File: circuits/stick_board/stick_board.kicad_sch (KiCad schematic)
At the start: 22 parts, among them J1 Conn_01x13_Pin, M2 Motor_DC, Q2 AO3400A, U1 GULI, U2 GULI, U5 DRV5055A1xDBZxQ1, U6 DRV5055A1xDBZxQ1

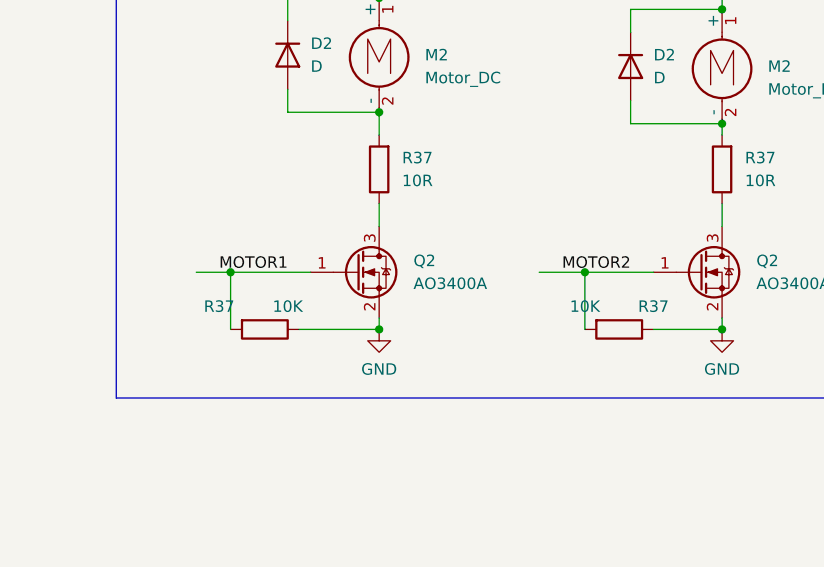
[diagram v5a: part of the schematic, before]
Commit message: 马达驱动增加栅极电阻
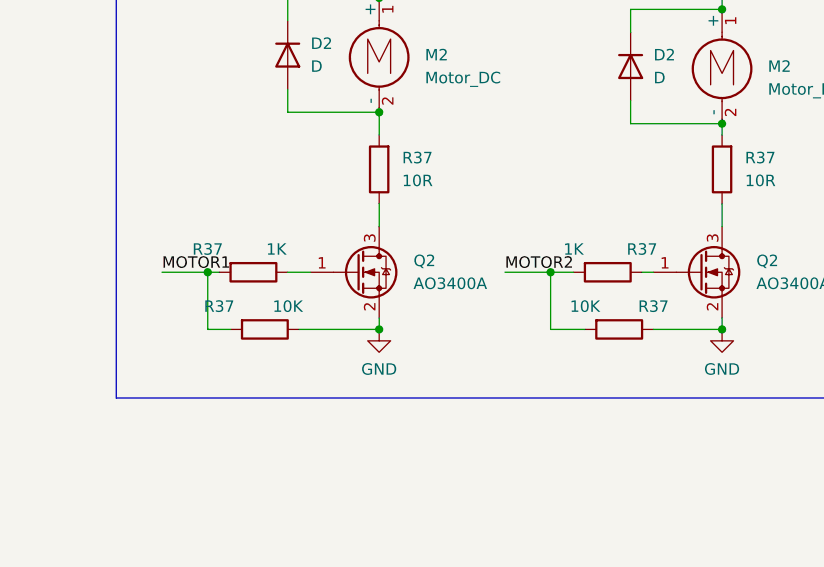
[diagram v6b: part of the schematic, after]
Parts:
- added R37 (x2): 1K, Resistor_SMD:R_0805_2012Metric_Pad1.20x1.40mm_HandSolder, symbol Device:R
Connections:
- net MOTOR1: now also R37.2; no longer Q2.1 (G)
- net MOTOR2: now also R37.2; no longer Q2.1 (G)
- new net: Q2.1 (G), R37.1 (x2)
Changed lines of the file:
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@@
   (junction (at 20.32 77.47) (diameter 0) (color 0 0 0 0)
   )
-  (junction (at 119.38 60.96) (diameter 0) (color 0 0 0 0)
-  )
   (junction (at 173.99 31.75) (diameter 0) (color 0 0 0 0)
   )
@@
   (junction (at 135.89 30.48) (diameter 0) (color 0 0 0 0)
   )
-  (junction (at 158.75 60.96) (diameter 0) (color 0 0 0 0)
-  )
   (junction (at 20.32 102.87) (diameter 0) (color 0 0 0 0)
   )
   (junction (at 135.89 43.18) (diameter 0) (color 0 0 0 0)
   )
+  (junction (at 116.84 60.96) (diameter 0) (color 0 0 0 0)
+  )
   (junction (at 135.89 67.31) (diameter 0) (color 0 0 0 0)
   )
@@
   (junction (at 19.05 48.26) (diameter 0) (color 0 0 0 0)
   )
+  (junction (at 154.94 60.96) (diameter 0) (color 0 0 0 0)
+  )
   (junction (at 29.21 21.59) (diameter 0) (color 0 0 0 0)
   )
   (junction (at 17.78 21.59) (diameter 0) (color 0 0 0 0)
   )
+  (wire (pts (xy 116.84 67.31) (xy 119.38 67.31))
+    (stroke (width 0) (type default))
+  )
+  (wire (pts (xy 154.94 67.31) (xy 158.75 67.31))
+    (stroke (width 0) (type default))
+  )
   (wire (pts (xy 53.34 93.98) (xy 53.34 102.87))
     (stroke (width 0) (type default))
@@
     (stroke (width 0) (type default))
   )
+  (wire (pts (xy 154.94 60.96) (xy 157.48 60.96))
+    (stroke (width 0) (type default))
+  )
   (wire (pts (xy 48.26 25.4) (xy 55.88 25.4))
     (stroke (width 0) (type default))
@@
     (stroke (width 0) (type default))
   )
-  (wire (pts (xy 115.57 60.96) (xy 119.38 60.96))
-    (stroke (width 0) (type default))
-  )
   (wire (pts (xy 30.48 180.34) (xy 52.07 180.34))
     (stroke (width 0) (type default))
@@
     (stroke (width 0) (type default))
   )
-  (wire (pts (xy 153.67 60.96) (xy 158.75 60.96))
-    (stroke (width 0) (type default))
-  )
-  (wire (pts (xy 158.75 60.96) (xy 158.75 67.31))
+  (wire (pts (xy 149.86 60.96) (xy 154.94 60.96))
+    (stroke (width 0) (type default))
+  )
+  (wire (pts (xy 154.94 60.96) (xy 154.94 67.31))
     (stroke (width 0) (type default))
   )
@@
     (stroke (width 0) (type default))
   )
-  (wire (pts (xy 119.38 60.96) (xy 128.27 60.96))
-    (stroke (width 0) (type default))
-  )
   (wire (pts (xy 29.21 21.59) (xy 29.21 16.51))
     (stroke (width 0) (type default))
@@
     (stroke (width 0) (type default))
   )
-  (wire (pts (xy 158.75 60.96) (xy 166.37 60.96))
-    (stroke (width 0) (type default))
-  )
   (wire (pts (xy 163.83 34.29) (xy 163.83 31.75))
     (stroke (width 0) (type default))
@@
     (stroke (width 0) (type default))
   )
+  (wire (pts (xy 111.76 60.96) (xy 116.84 60.96))
+    (stroke (width 0) (type default))
+  )
   (wire (pts (xy 30.48 160.02) (xy 52.07 160.02))
     (stroke (width 0) (type default))
@@
     (stroke (width 0) (type default))
   )
+  (wire (pts (xy 116.84 60.96) (xy 118.11 60.96))
+    (stroke (width 0) (type default))
+  )
   (wire (pts (xy 59.69 99.06) (xy 59.69 102.87))
     (stroke (width 0) (type default))
@@
     (stroke (width 0) (type default))
   )
-  (wire (pts (xy 119.38 67.31) (xy 119.38 60.96))
+  (wire (pts (xy 116.84 67.31) (xy 116.84 60.96))
     (stroke (width 0) (type default))
   )
@@
     (stroke (width 0) (type default))
   )
+  (wire (pts (xy 125.73 60.96) (xy 128.27 60.96))
+    (stroke (width 0) (type default))
+  )
   (wire (pts (xy 30.48 172.72) (xy 52.07 172.72))
+    (stroke (width 0) (type default))
+  )
+  (wire (pts (xy 165.1 60.96) (xy 166.37 60.96))
     (stroke (width 0) (type default))
   )
@@
     (effects (font (size 1.27 1.27)) (justify right bottom))
   )
-  (label "MOTOR1" (at 118.11 60.96 0) (fields_autoplaced)
+  (label "MOTOR1" (at 111.76 60.96 0) (fields_autoplaced)
     (effects (font (size 1.27 1.27)) (justify left bottom))
   )
@@
     (effects (font (size 1.27 1.27)) (justify left bottom))
   )
-  (label "MOTOR2" (at 156.21 60.96 0) (fields_autoplaced)
+  (label "MOTOR2" (at 149.86 60.96 0) (fields_autoplaced)
     (effects (font (size 1.27 1.27)) (justify left bottom))
   )
@@
     )
   )
+  (symbol (lib_id "Device:R") (at 161.29 60.96 270) (unit 1)
+    (in_bom yes) (on_board yes) (dnp no)
+    (property "Reference" "R37" (at 165.1 58.42 90)
+      (effects (font (size 1.27 1.27)))
+    )
+    (property "Value" "1K" (at 157.48 58.42 90)
+      (effects (font (size 1.27 1.27)))
+    )
+    (property "Footprint" "Resistor_SMD:R_0805_2012Metric_Pad1.20x1.40mm_HandSolder" (at 161.29 59.182 90)
+      (effects (font (size 1.27 1.27)) hide)
+    )
+    (property "Datasheet" "~" (at 161.29 60.96 0)
+      (effects (font (size 1.27 1.27)) hide)
+    )
+    (pin "1")
+    (pin "2")
+    (instances
+      (project "testpad"
+        (path "/2275f0ad-bf55-4256-a734-efa72019bc53"
+          (reference "R37") (unit 1)
+        )
+      )
+      (project "stick_board"
+        (path "/ee025c96-6b34-4741-98da-90887f64560f"
+          (reference "R4") (unit 1)
+        )
+      )
+    )
+  )
   (symbol (lib_id "power:+3V3") (at 20.32 77.47 0) (unit 1)
     (in_bom yes) (on_board yes) (dnp no) (fields_autoplaced)
@@
         )
       )
+    )
+  )
+  (symbol (lib_id "Device:R") (at 121.92 60.96 270) (unit 1)
+    (in_bom yes) (on_board yes) (dnp no)
+    (property "Reference" "R37" (at 116.84 58.42 90)
+      (effects (font (size 1.27 1.27)))
+    )
+    (property "Value" "1K" (at 124.46 58.42 90)
+      (effects (font (size 1.27 1.27)))
+    )
+    (property "Footprint" "Resistor_SMD:R_0805_2012Metric_Pad1.20x1.40mm_HandSolder" (at 121.92 59.182 90)
+      (effects (font (size 1.27 1.27)) hide)
+    )
+    (property "Datasheet" "~" (at 121.92 60.96 0)
+      (effects (font (size 1.27 1.27)) hide)
+    )
+    (pin "1")
+    (pin "2")
+    (instances
+      (project "testpad"
+        (path "/2275f0ad-bf55-4256-a734-efa72019bc53"
+          (reference "R37") (unit 1)
+        )
+      )
+      (project "stick_board"
+        (path "/ee025c96-6b34-4741-98da-90887f64560f"
+          (reference "R3") (unit 1)
+        )
+      )

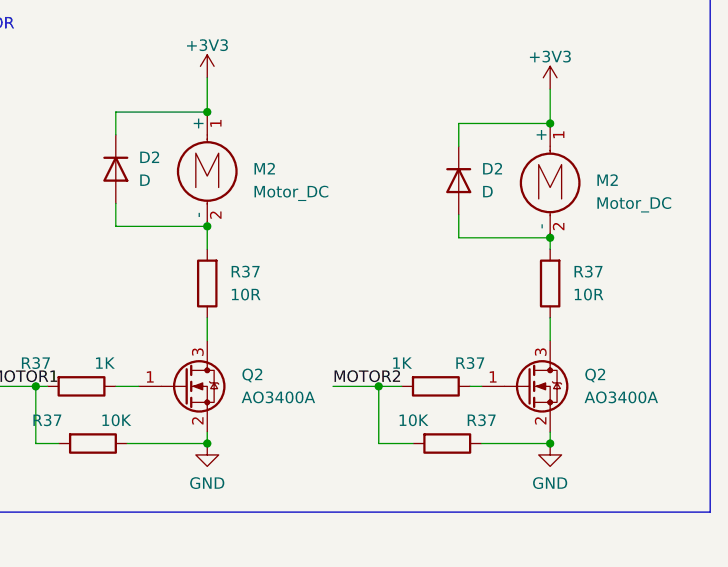
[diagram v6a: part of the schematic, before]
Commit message: stick板去除马达限流电阻
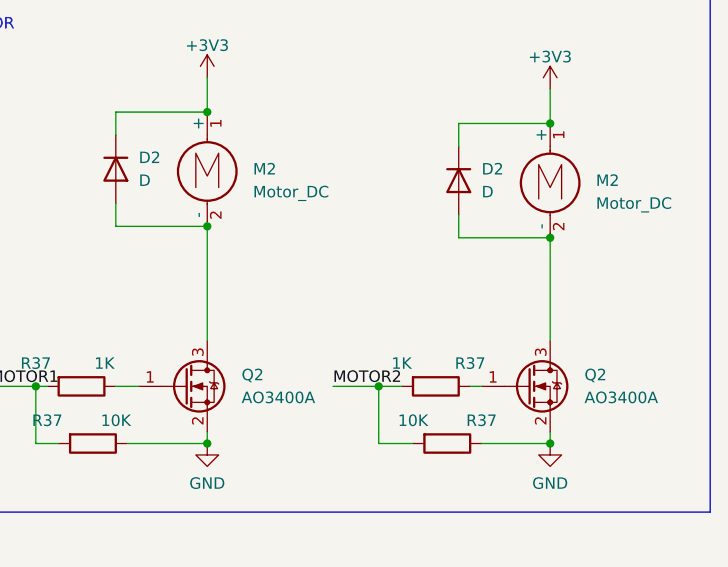
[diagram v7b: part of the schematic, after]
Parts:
- removed R37 (x2): 10R, Resistor_SMD:R_1206_3216Metric_Pad1.30x1.75mm_HandSolder, symbol Device:R
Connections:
- net at D2.2 (A), M2.2 (-): now also Q2.3 (D) (x2)
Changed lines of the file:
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@@
     (stroke (width 0) (type default))
   )
-  (wire (pts (xy 135.89 53.34) (xy 135.89 55.88))
+  (wire (pts (xy 135.89 43.18) (xy 135.89 55.88))
     (stroke (width 0) (type default))
   )
@@
     (stroke (width 0) (type default))
   )
-  (wire (pts (xy 173.99 45.72) (xy 173.99 44.45))
-    (stroke (width 0) (type default))
-  )
   (wire (pts (xy 27.94 77.47) (xy 20.32 77.47))
     (stroke (width 0) (type default))
@@
     (stroke (width 0) (type default))
   )
-  (wire (pts (xy 173.99 53.34) (xy 173.99 55.88))
+  (wire (pts (xy 173.99 44.45) (xy 173.99 55.88))
     (stroke (width 0) (type default))
   )
@@
   )
   (wire (pts (xy 30.48 177.8) (xy 52.07 177.8))
-    (stroke (width 0) (type default))
-  )
-  (wire (pts (xy 135.89 43.18) (xy 135.89 45.72))
     (stroke (width 0) (type default))
   )
@@
     )
   )
-  (symbol (lib_id "Device:R") (at 135.89 49.53 180) (unit 1)
-    (in_bom yes) (on_board yes) (dnp no) (fields_autoplaced)
-    (property "Reference" "R37" (at 138.43 48.26 0)
-      (effects (font (size 1.27 1.27)) (justify right))
-    )
-    (property "Value" "10R" (at 138.43 50.8 0)
-      (effects (font (size 1.27 1.27)) (justify right))
-    )
-    (property "Footprint" "Resistor_SMD:R_1206_3216Metric_Pad1.30x1.75mm_HandSolder" (at 137.668 49.53 90)
-      (effects (font (size 1.27 1.27)) hide)
-    )
-    (property "Datasheet" "~" (at 135.89 49.53 0)
-      (effects (font (size 1.27 1.27)) hide)
-    )
-    (pin "1")
-    (pin "2")
-    (instances
-      (project "testpad"
-        (path "/2275f0ad-bf55-4256-a734-efa72019bc53"
-          (reference "R37") (unit 1)
-        )
-      )
-      (project "stick_board"
-        (path "/ee025c96-6b34-4741-98da-90887f64560f"
-          (reference "R20") (unit 1)
-        )
-      )
-    )
-  )
   (symbol (lib_id "power:PWR_FLAG") (at 38.1 152.4 0) (unit 1)
     (in_bom yes) (on_board yes) (dnp no) (fields_autoplaced)
@@
         )
       )
-    )
-  )
-  (symbol (lib_id "Device:R") (at 173.99 49.53 180) (unit 1)
-    (in_bom yes) (on_board yes) (dnp no) (fields_autoplaced)
-    (property "Reference" "R37" (at 176.53 48.26 0)
-      (effects (font (size 1.27 1.27)) (justify right))
-    )
-    (property "Value" "10R" (at 176.53 50.8 0)
-      (effects (font (size 1.27 1.27)) (justify right))
-    )
-    (property "Footprint" "Resistor_SMD:R_1206_3216Metric_Pad1.30x1.75mm_HandSolder" (at 175.768 49.53 90)
-      (effects (font (size 1.27 1.27)) hide)
-    )
-    (property "Datasheet" "~" (at 173.99 49.53 0)
-      (effects (font (size 1.27 1.27)) hide)
-    )
-    (pin "1")
-    (pin "2")
-    (instances
-      (project "testpad"
-        (path "/2275f0ad-bf55-4256-a734-efa72019bc53"
-          (reference "R37") (unit 1)
-        )
-      )
-      (project "stick_board"
-        (path "/ee025c96-6b34-4741-98da-90887f64560f"
-          (reference "R21") (unit 1)
-        )
-      )
